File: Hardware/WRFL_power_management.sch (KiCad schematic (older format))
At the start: 27 parts

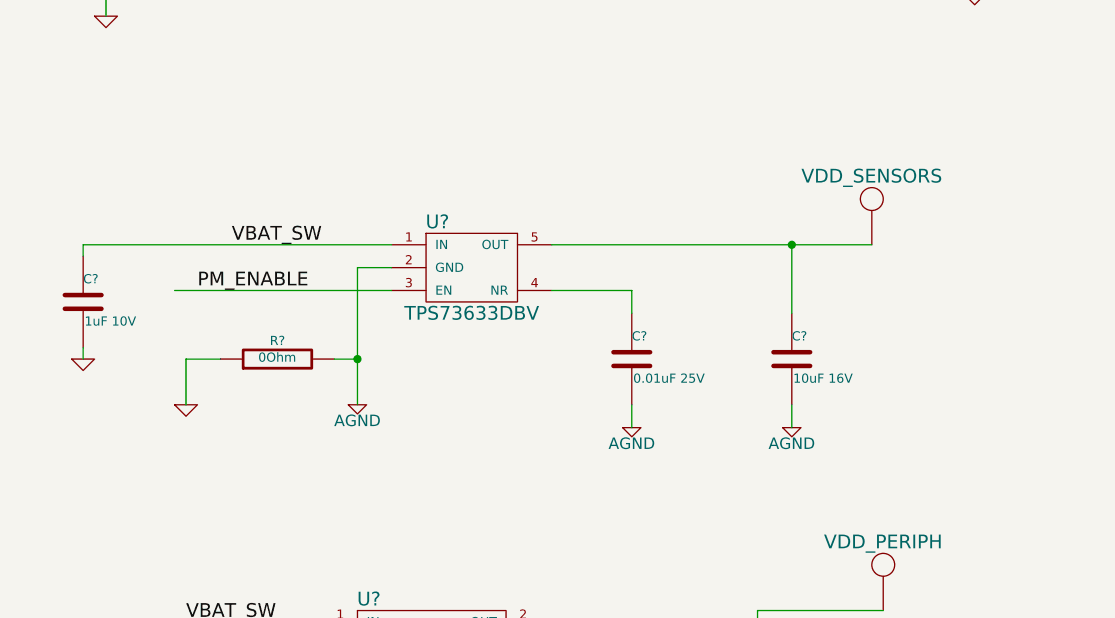
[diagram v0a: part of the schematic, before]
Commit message: moved sensor LDO
to sensor sheet
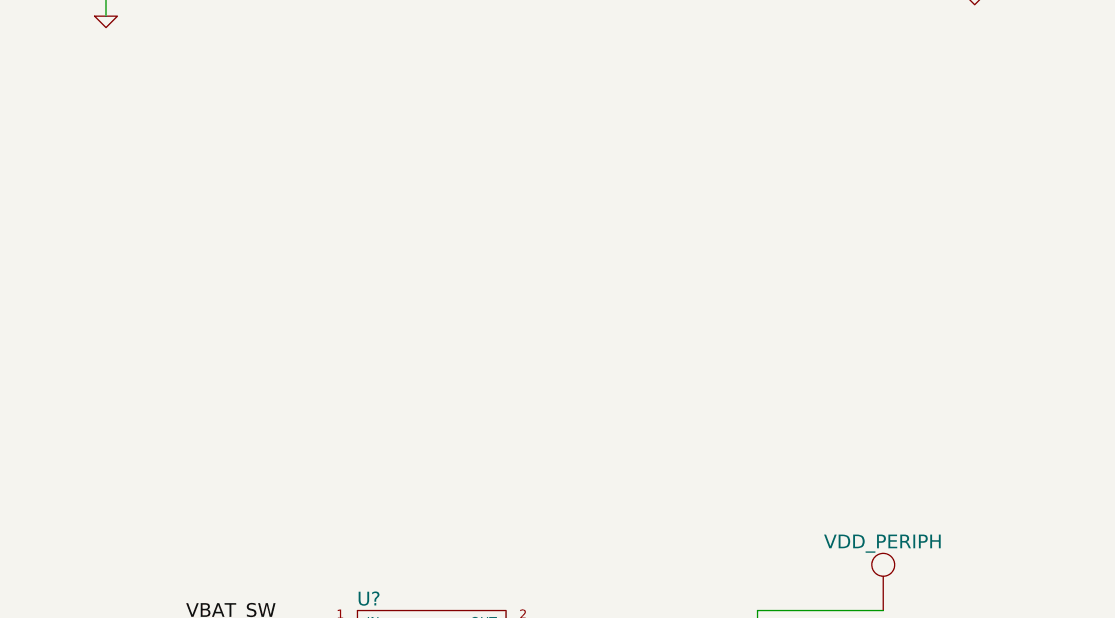
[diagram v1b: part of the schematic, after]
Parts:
- removed C?: 0.01uF 25V, ~, symbol C
- removed C?: 10uF 16V, ~, symbol C
- removed C?: 1uF 10V, ~, symbol C
- removed R?: 0Ohm, ~, symbol R
- removed U?: TPS73633DBV, symbol TPS73633DBV
- removed U?: VDD_SENSORS, symbol VDD_SENSORS
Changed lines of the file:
@@
-EESchema Schematic File Version 2  date 10/2/2013 1:05:42 AM
+EESchema Schematic File Version 2  date Thursday, October 03, 2013 02:41:38 PM
 LIBS:power
 LIBS:device
@@
 Sheet 2 5
 Title "WRFL power management"
-Date "1 oct 2013"
+Date "3 oct 2013"
 Rev "1.0"
 Comp "Nightmechanic"
@@
 	8400 1800 8400 2000
 $Comp
-L TPS73633DBV U?
-U 1 1 524B391F
-P 2900 4400
-F 0 "U?" H 2750 4600 60  0000 C CNN
-F 1 "TPS73633DBV" H 2900 4200 60  0000 C CNN
-F 2 "" H 2900 4400 60  0000 C CNN
-F 3 "http://www.ti.com/lit/ds/symlink/tps73633.pdf" H 2950 4100 60  0001 C CNN
-	1    2900 4400
-	1    0    0    -1
-$EndComp
-Wire Wire Line
-	1200 4300 2550 4300
-Text Label 1850 4300 0    60   ~ 0
-VBAT_SW
-Wire Wire Line
-	2550 4500 1600 4500
-Wire Wire Line
-	3250 4300 4650 4300
-$Comp
-L C C?
-U 1 1 524B39BC
-P 3600 4800
-F 0 "C?" H 3600 4900 40  0000 L CNN
-F 1 "0.01uF 25V" H 3606 4715 40  0000 L CNN
-F 2 "~" H 3638 4650 30  0000 C CNN
-F 3 "~" H 3600 4800 60  0000 C CNN
-	1    3600 4800
-	1    0    0    -1
-$EndComp
-Wire Wire Line
-	3250 4500 3600 4500
-Wire Wire Line
-	3600 4500 3600 4600
-$Comp
-L C C?
-U 1 1 524B3A2B
-P 4300 4800
-F 0 "C?" H 4300 4900 40  0000 L CNN
-F 1 "10uF 16V" H 4306 4715 40  0000 L CNN
-F 2 "~" H 4338 4650 30  0000 C CNN
-F 3 "~" H 4300 4800 60  0000 C CNN
-	1    4300 4800
-	1    0    0    -1
-$EndComp
-Wire Wire Line
-	4300 4300 4300 4600
-Connection ~ 4300 4300
-$Comp
-L AGND #PWR?
-U 1 1 524B3BD6
-P 3600 5100
-F 0 "#PWR?" H 3600 5100 40  0001 C CNN
-F 1 "AGND" H 3600 5030 50  0000 C CNN
-F 2 "" H 3600 5100 60  0000 C CNN
-F 3 "" H 3600 5100 60  0000 C CNN
-	1    3600 5100
-	1    0    0    -1
-$EndComp
-$Comp
-L AGND #PWR?
-U 1 1 524B3BE5
-P 4300 5100
-F 0 "#PWR?" H 4300 5100 40  0001 C CNN
-F 1 "AGND" H 4300 5030 50  0000 C CNN
-F 2 "" H 4300 5100 60  0000 C CNN
-F 3 "" H 4300 5100 60  0000 C CNN
-	1    4300 5100
-	1    0    0    -1
-$EndComp
-$Comp
-L AGND #PWR?
-U 1 1 524B3BF4
-P 2400 5000
-F 0 "#PWR?" H 2400 5000 40  0001 C CNN
-F 1 "AGND" H 2400 4930 50  0000 C CNN
-F 2 "" H 2400 5000 60  0000 C CNN
-F 3 "" H 2400 5000 60  0000 C CNN
-	1    2400 5000
-	1    0    0    -1
-$EndComp
-$Comp
-L GND #PWR?
-U 1 1 524B3C03
-P 1650 5000
-F 0 "#PWR?" H 1650 5000 30  0001 C CNN
-F 1 "GND" H 1650 4930 30  0001 C CNN
-F 2 "" H 1650 5000 60  0000 C CNN
-F 3 "" H 1650 5000 60  0000 C CNN
-	1    1650 5000
-	1    0    0    -1
-$EndComp
-Wire Wire Line
-	4300 5000 4300 5100
-Wire Wire Line
-	3600 5000 3600 5100
-Wire Wire Line
-	2550 4400 2400 4400
-Wire Wire Line
-	2400 4400 2400 5000
-$Comp
-L R R?
-U 1 1 524B3CB1
-P 2050 4800
-F 0 "R?" V 2130 4800 40  0000 C CNN
-F 1 "0Ohm" V 2057 4801 40  0000 C CNN
-F 2 "~" V 1980 4800 30  0000 C CNN
-F 3 "~" H 2050 4800 30  0000 C CNN
-	1    2050 4800
-	0    -1   -1   0
-$EndComp
-Wire Wire Line
-	2300 4800 2400 4800
-Connection ~ 2400 4800
-Wire Wire Line
-	1800 4800 1650 4800
-Wire Wire Line
-	1650 4800 1650 5000
-$Comp
 L TPS73633DCQ U?
 U 1 1 524B3D49
@@
 $Comp
 L C C?
-U 1 1 524B3D8B
-P 1200 4550
-F 0 "C?" H 1200 4650 40  0000 L CNN
-F 1 "1uF 10V" H 1206 4465 40  0000 L CNN
-F 2 "~" H 1238 4400 30  0000 C CNN
-F 3 "~" H 1200 4550 60  0000 C CNN
-	1    1200 4550
-	1    0    0    -1
-$EndComp
-$Comp
-L C C?
 U 1 1 524B3D91
 P 1300 6200
@@
 $Comp
 L GND #PWR?
-U 1 1 524B3EF1
-P 1200 4800
-F 0 "#PWR?" H 1200 4800 30  0001 C CNN
-F 1 "GND" H 1200 4730 30  0001 C CNN
-F 2 "" H 1200 4800 60  0000 C CNN
-F 3 "" H 1200 4800 60  0000 C CNN
-	1    1200 4800
-	1    0    0    -1
-$EndComp
-$Comp
-L GND #PWR?
 U 1 1 524B3F00
 P 1300 6450
@@
 Wire Wire Line
 	1300 5950 1300 6000
-Wire Wire Line
-	1200 4300 1200 4350
-Wire Wire Line
-	1200 4750 1200 4800
 Text Label 1650 5950 0    60   ~ 0
 VBAT_SW
-Text Label 1700 4500 0    60   ~ 0
-PM_ENABLE
 Wire Wire Line
 	2250 6100 1550 6100
@@
 	1    0    0    -1
 $EndComp
-$Comp
-L VDD_SENSORS U?
-U 1 1 524B449F
-P 4650 4100
-F 0 "U?" H 4650 4300 60  0001 C CNN
-F 1 "VDD_SENSORS" H 4650 4200 60  0000 C CNN
-F 2 "" H 4650 4100 60  0000 C CNN
-F 3 "" H 4650 4100 60  0000 C CNN
-	1    4650 4100
-	1    0    0    -1
-$EndComp
